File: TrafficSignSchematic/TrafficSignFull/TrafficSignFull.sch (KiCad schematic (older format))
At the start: 29 parts, among them J1 IDC connector, J2 3.96mm pitch 4-pin polarized 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, SW1 Power switch, U1 ATmega328P-PU, U2 SIM800L, U3 BQ24650, Y1 16MHz

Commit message: PCB elements import
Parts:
- C1, C2: footprint (none) -> Capacitor_THT:C_Disc_D4.3mm_W1.9mm_P5.00mm
- U3: symbol TrafficSign-rescue:BQ24650-Battery_Management -> CustomSymbols:BQ24650-MPPT-Controller
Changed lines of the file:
@@
 Connection ~ 3150 4650
 $Comp
-L TrafficSign-rescue:BQ24650-Battery_Management U3
+L CustomSymbols:BQ24650-MPPT-Controller U3
 U 1 1 5E1C2763
 P 2450 1250
@@
 F 0 "C2" V 3300 4750 50  0000 C CNN
 F 1 "22pF" V 3400 4800 50  0000 C CNN
-F 2 "" H 3388 4500 50  0001 C CNN
+F 2 "Capacitor_THT:C_Disc_D4.3mm_W1.9mm_P5.00mm" H 3388 4500 50  0001 C CNN
 F 3 "https://store.comet.bg/Catalogue/Product/27466/" H 3350 4650 50  0001 C CNN
 	1    3350 4650
@@
 F 0 "C1" V 3300 4450 50  0000 C CNN
 F 1 "22pF" V 3400 4500 50  0000 C CNN
-F 2 "" H 3388 4200 50  0001 C CNN
+F 2 "Capacitor_THT:C_Disc_D4.3mm_W1.9mm_P5.00mm" H 3388 4200 50  0001 C CNN
 F 3 "https://store.comet.bg/Catalogue/Product/27466/" H 3350 4350 50  0001 C CNN
 	1    3350 4350

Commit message: Updated full schematic
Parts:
- removed R5: 10k, Resistor_THT:R_Axial_DIN0204_L3.6mm_D1.6mm_P7.62mm_Horizontal, symbol Device:R
- added C3, C4, C5, C6, C7: 100n, Capacitor_THT:C_Disc_D4.3mm_W1.9mm_P5.00mm, symbol Device:C
- added H1, H2, H3, H4: MountingHole, MountingHole:MountingHole_3.2mm_M3_ISO14580, symbol Mechanical:MountingHole
- added J3: Power input, Connector_Molex:Molex_KK-396_A-41791-0004_1x04_P3.96mm_Vertical, symbol Connector_Generic:Conn_01x04
- added R6, R7: 10k, Resistor_THT:R_Axial_DIN0204_L3.6mm_D1.6mm_P7.62mm_Horizontal, symbol Device:R
- COUT1, COUT2: footprint Capacitor_THT:CP_Radial_D10.0mm_P5.00mm -> Capacitor_THT:CP_Radial_D8.0mm_P3.50mm
- D1, D2: footprint Diode_THT:D_DO-27_P15.24mm_Horizontal -> Diode_THT:D_DO-27_P12.70mm_Horizontal
- J1: value IDC connector -> LED matrix data
- J2: value 3.96mm pitch 4-pin polarized connector -> LED matrix power
- R4: value 10k -> 20k
- U2: symbol SIM800L:SIM800L -> TrafficSignPCB-rescue:SIM800L-SIM800L
- renumbered R6 to R5
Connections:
- net +12V: now also J3.1 (Pin_1), J3.2 (Pin_2)
- net +4V: now also C6.1
- net +5V: now also C4.1, C5.1, C7.1; no longer U1.21 (AREF)
- net 8: now also R7.1
- net GND: now also R4.2, C3.2, C4.2, C5.2, C6.2, C7.2, J3.3 (Pin_3), J3.4 (Pin_4)
- net RXD: now also R6.1; no longer U2.5 (TXD)
- net SIM_RST: now reaches U2.3 (RST)
- net SIM_RST: now also R7.2
- new net: C3.1, U1.21 (AREF)
- new net: R6.2, U2.5 (TXD)
- no-connect marks 12 -> 10
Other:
- moved on the sheet: AE1, BT1, C1, C2, CFF1, CIN1, CIN2, COUT1, COUT2, D1, D2, J1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

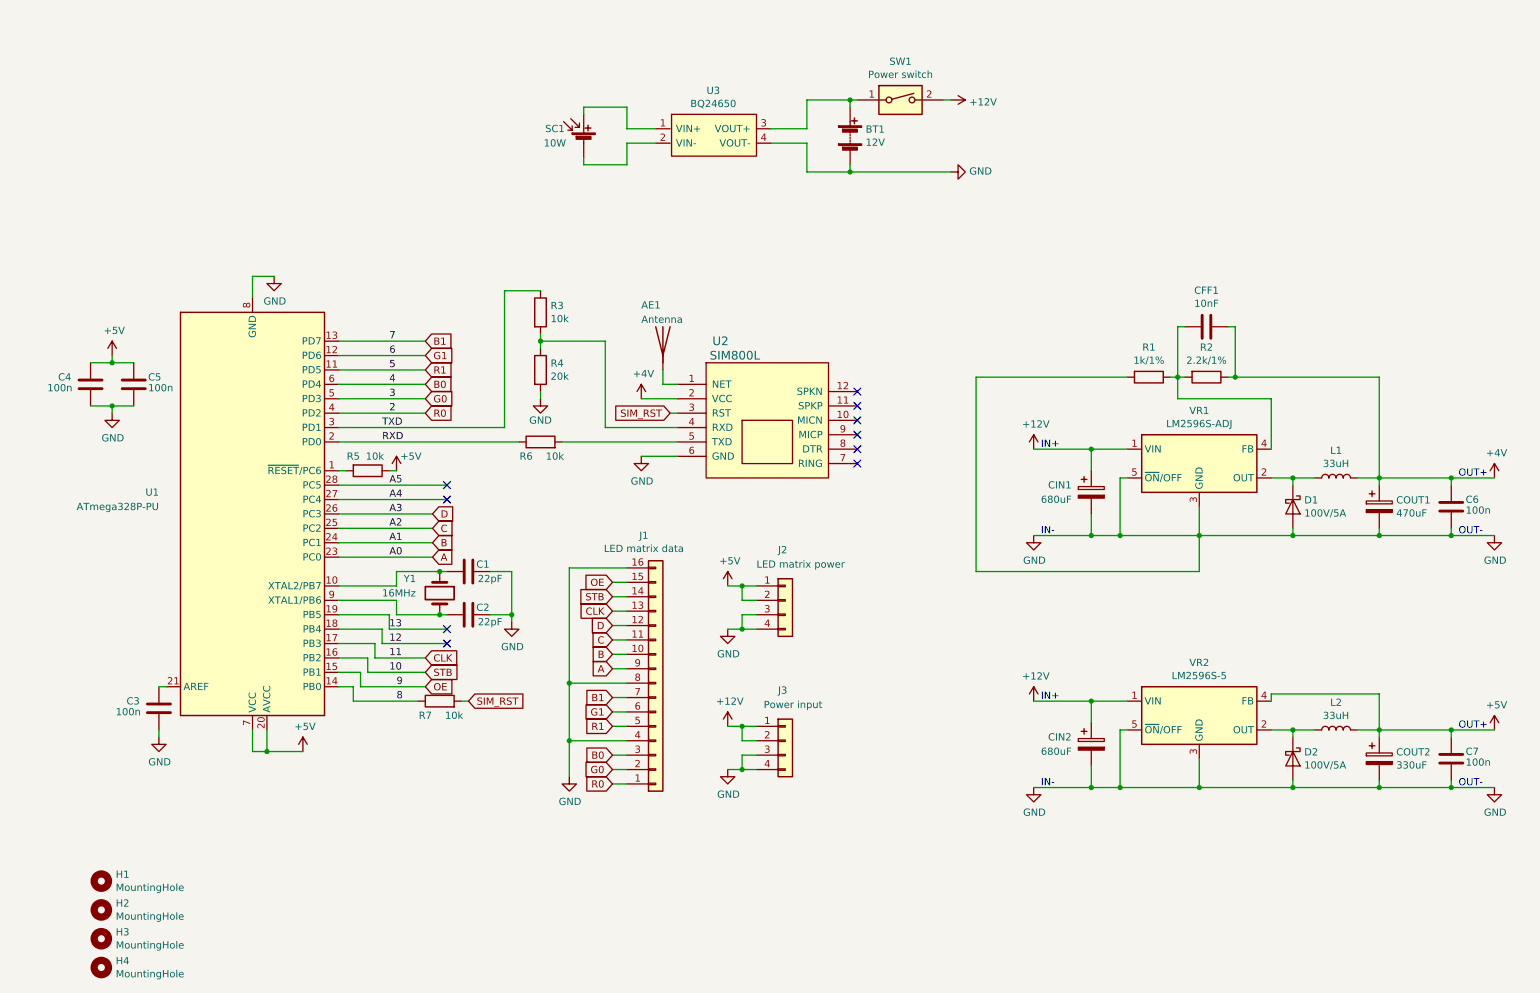
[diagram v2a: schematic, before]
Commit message: Seperated schematic into blocks
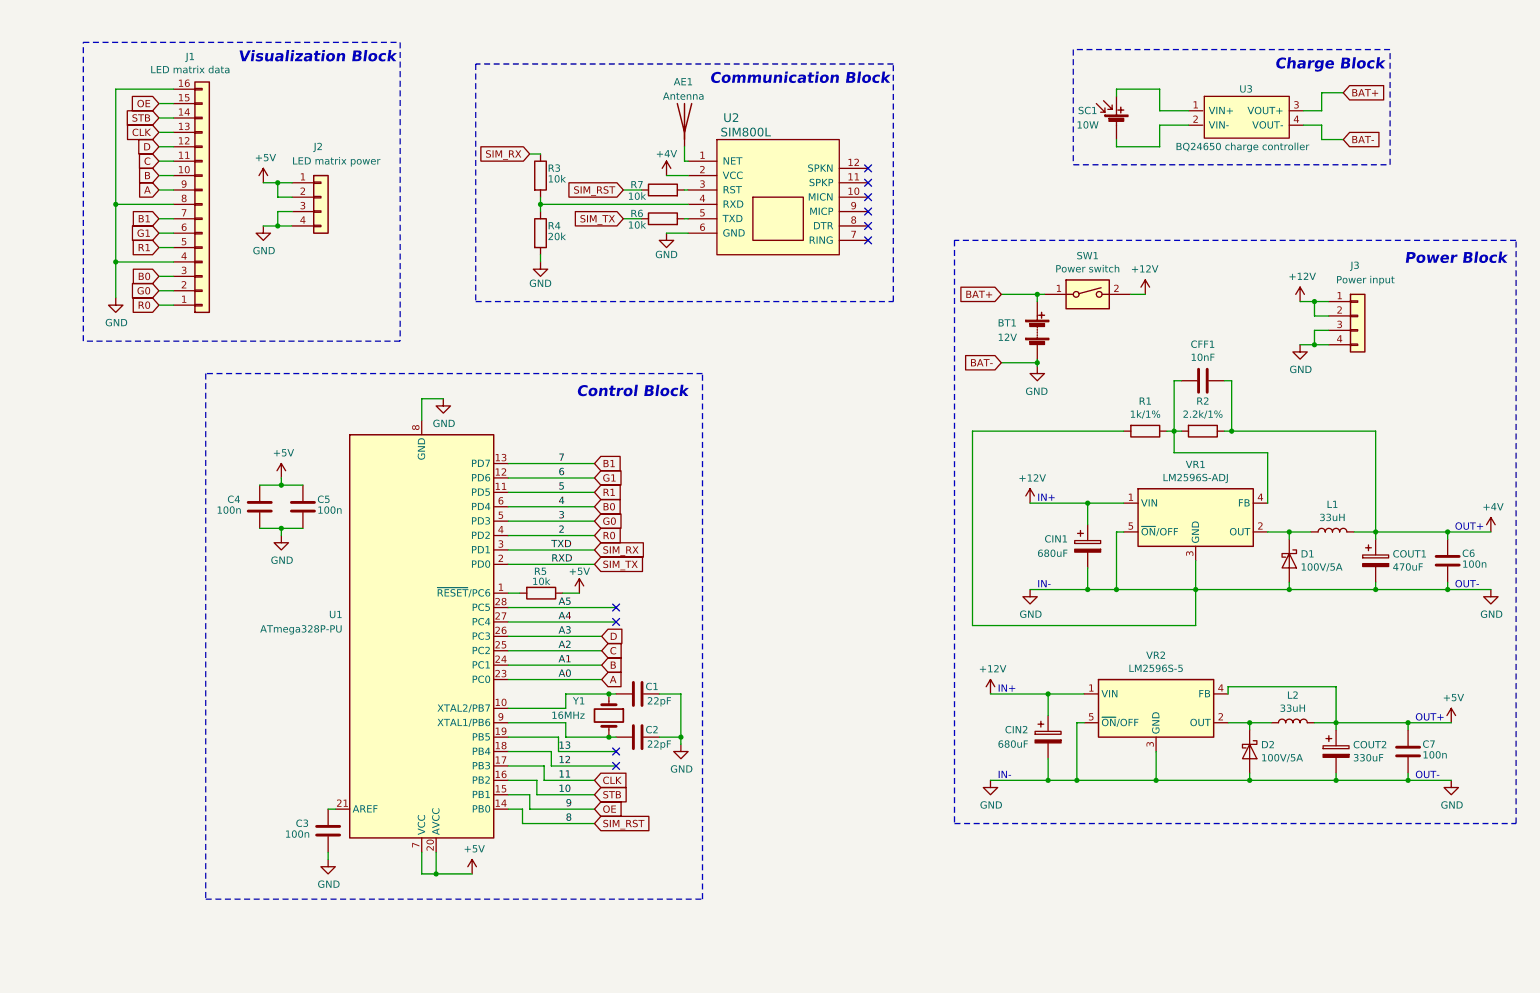
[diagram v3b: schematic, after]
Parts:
- removed H1, H2, H3, H4: MountingHole, MountingHole:MountingHole_3.2mm_M3_ISO14580, symbol Mechanical:MountingHole
- U3: value BQ24650 -> BQ24650 charge controller
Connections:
- net 8 is gone; now on net SIM_RST: R7.1, U1.14 (PB0)
- net SIM_RST: no longer R7.2, U2.3 (RST)
- net BAT+: now reaches BT1.1 (+), SW1.1, U3.3 (VOUT+)
- net RXD renamed SIM_TX
- net TXD renamed SIM_RX
- new net: R7.2, U2.3 (RST)
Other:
- note added: "Charge Block"
- note added: "Communication Block"
- note added: "Control Block"
- note added: "Power Block"
- note added: "Visualization Block"
- moved on the sheet: AE1, BT1, C1, C2, C3, C4, C5, C6, C7, CFF1, CIN1, CIN2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

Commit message: Reordered some stuff and fixed a resistor value
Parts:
- R3: value 10k -> 16k
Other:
- moved on the sheet: C1, C2, C3, C4, C5, C7, CIN2, COUT2, D2, L2, R5, U1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
